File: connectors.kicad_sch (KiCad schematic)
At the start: 13 parts, among them J1 RCJ-017, J2 USB4105-GF-A-120, J3 Conn_01x02_Pin, J4 Conn_01x02_Pin

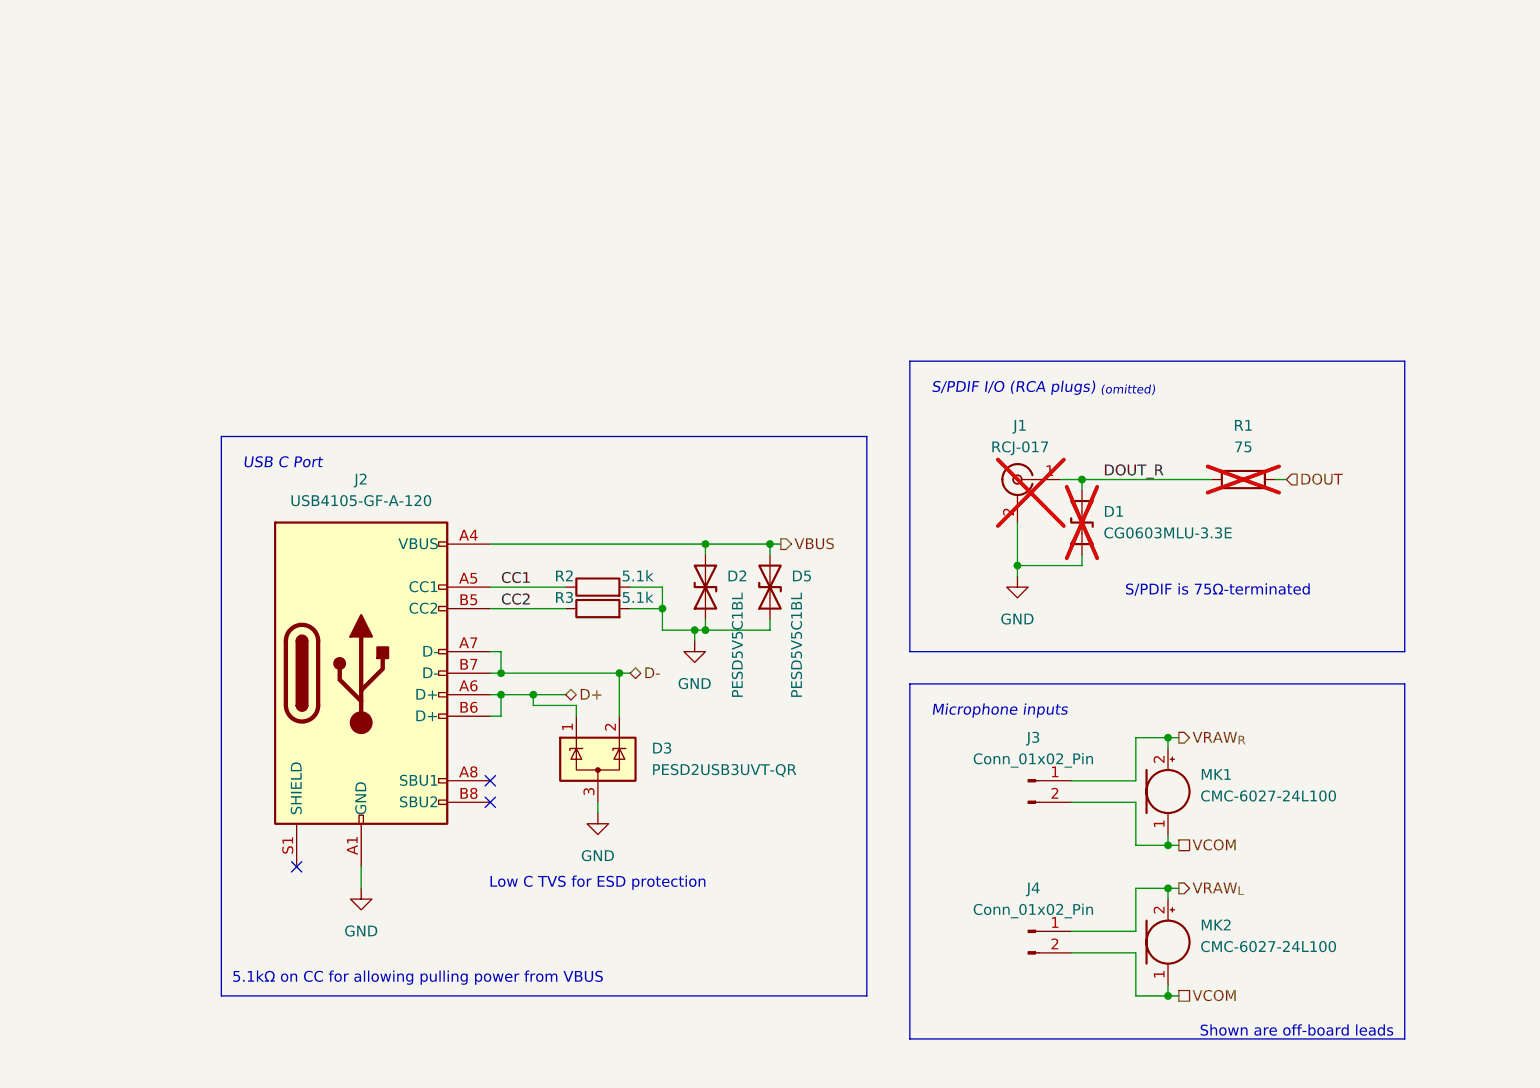
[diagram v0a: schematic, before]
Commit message: Redid schematic and component values according to new recalculations
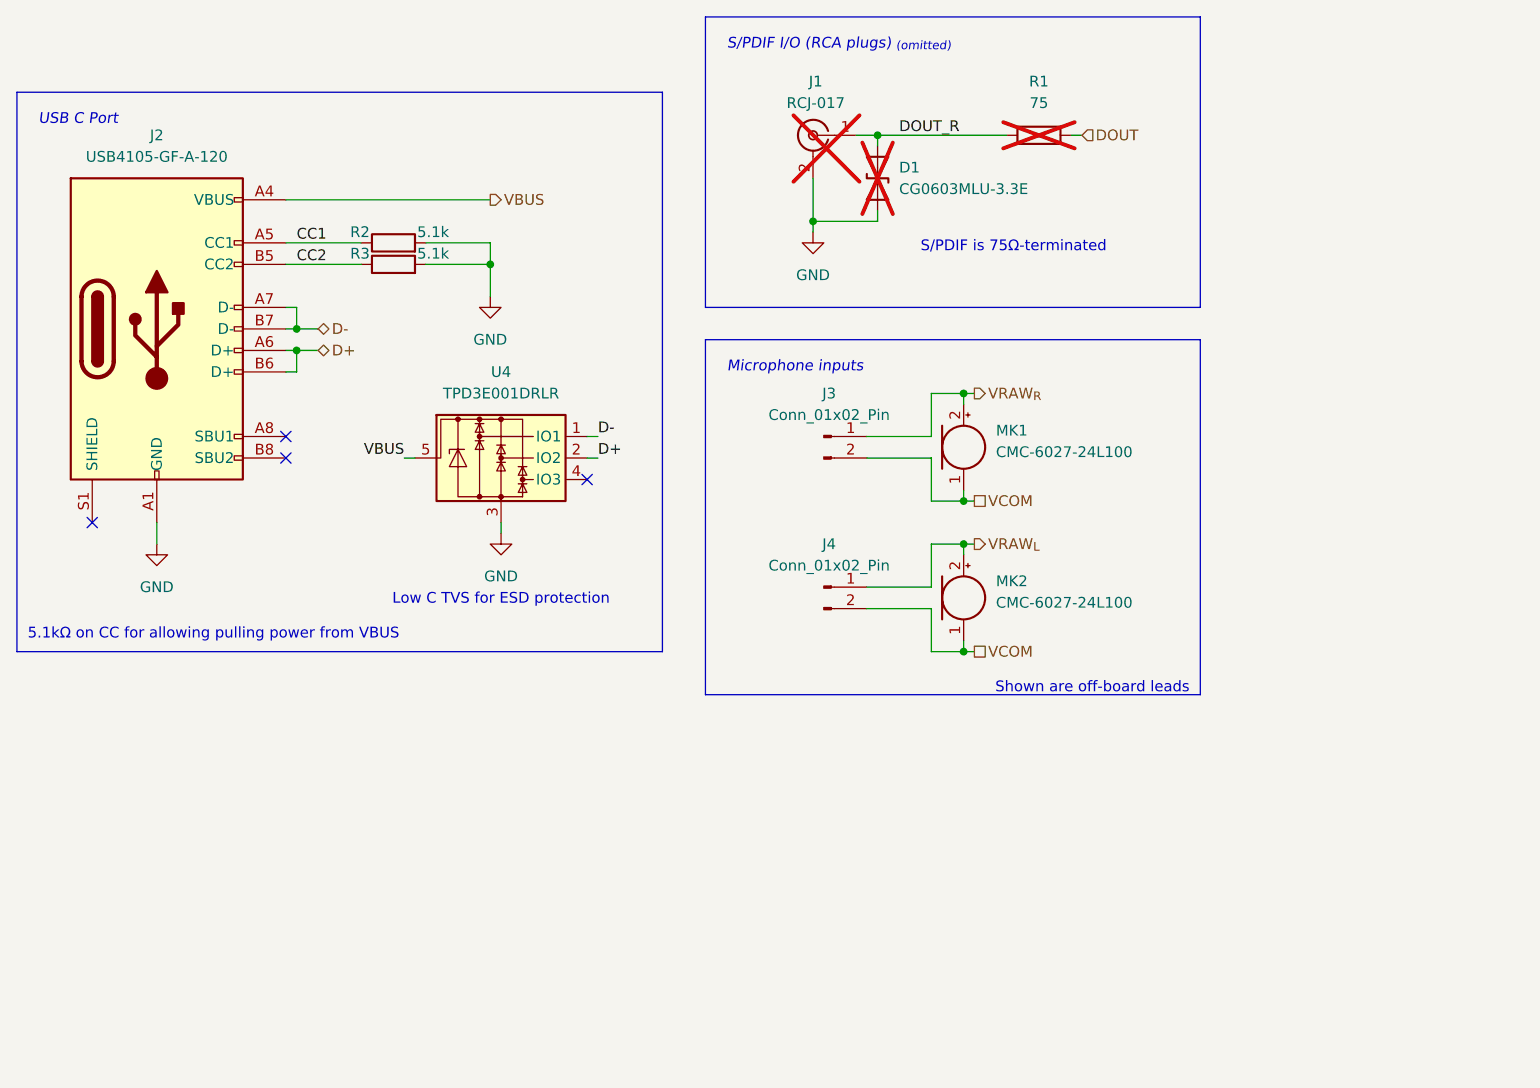
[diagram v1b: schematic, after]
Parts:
- removed D2, D5: PESD5V5C1BL, Diode_SMD:D_SOD-882, symbol Device:D_TVS
- removed D3: PESD2USB3UVT-QR, Package_TO_SOT_SMD:SOT-23-3, symbol Power_Protection:ESDA5V3L
- added U4: TPD3E001DRLR, Package_TO_SOT_SMD:SOT-553, symbol Power_Protection:TPD3E001DRLR
- J2: footprint Connector_USB:USB_C_Receptacle_GCT_USB4105-xx-A_16P_TopMnt_Horizontal -> Connector_USB:USB_C_Receptacle_GCT_USB4085; Mouser Part Number 640-USB4105-GF-A-120 -> 640-USB4085-GF-A
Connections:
- net D+: now also U4.2 (IO2)
- net D-: now also U4.1 (IO1)
- net GND: now also U4.3
- net VBUS: now also U4.5
- no-connect marks 3 -> 4
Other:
- moved on the sheet: D1, J1, J2, J3, J4, MK1, MK2, R1, R2, R3

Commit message: Add buttons for device control + various other changes
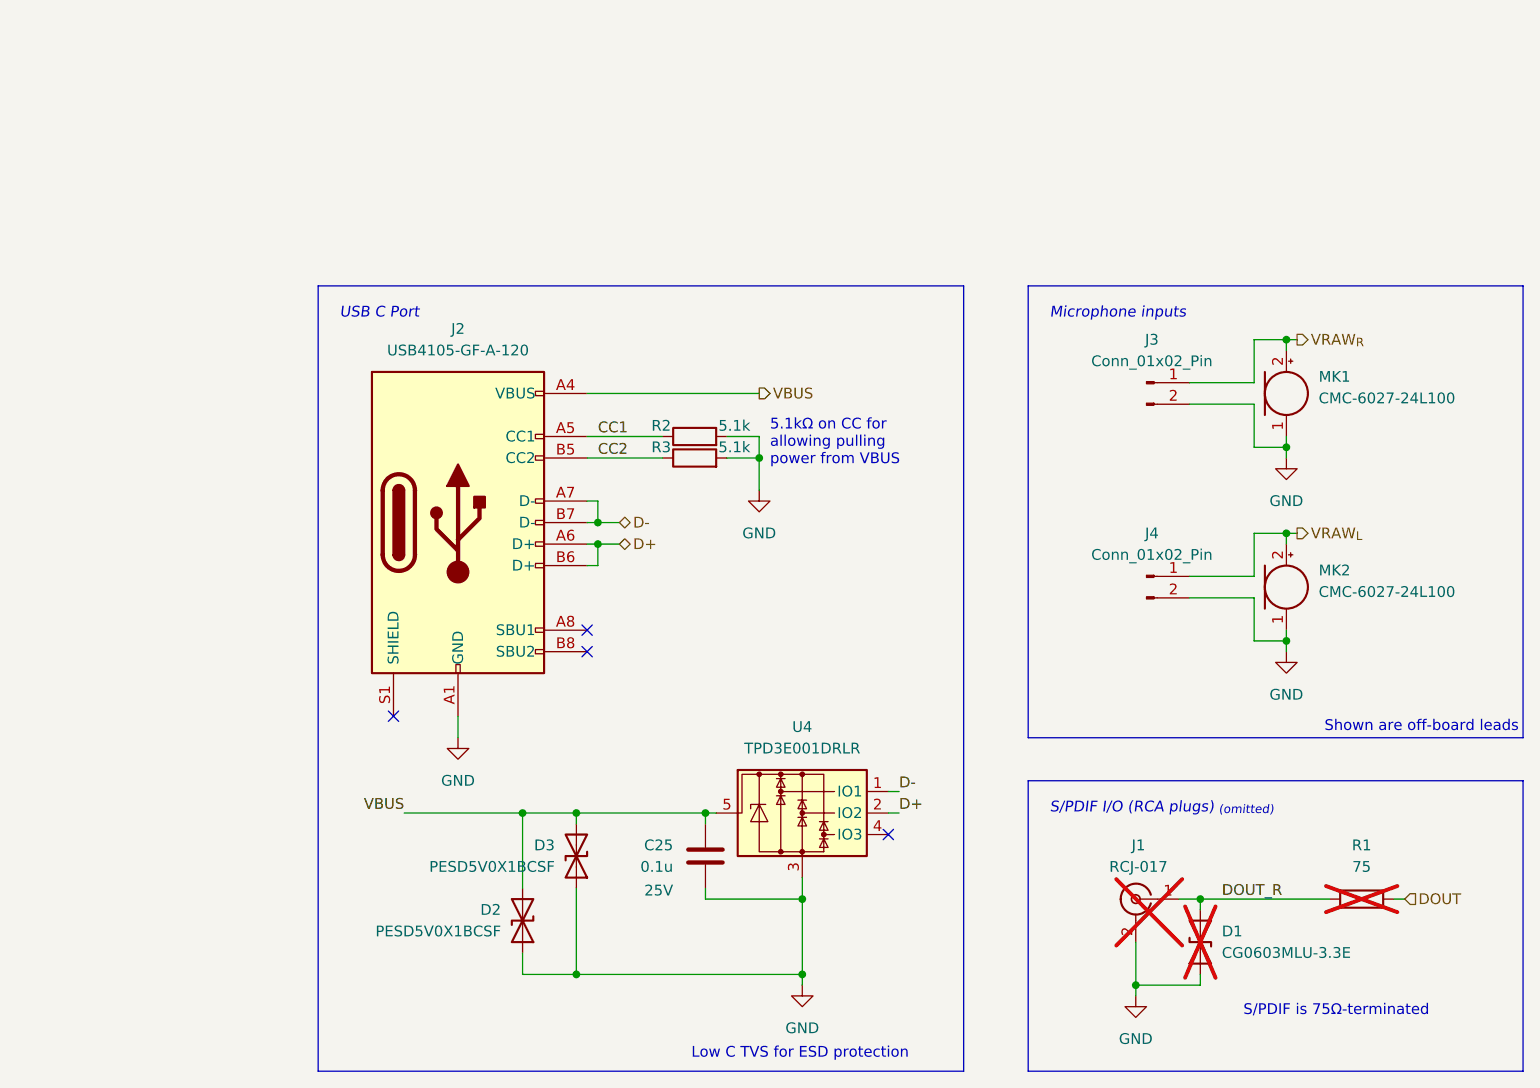
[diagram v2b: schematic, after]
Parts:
- added C25: 0.1u, Capacitor_SMD:C_0603_1608Metric_Pad1.08x0.95mm_HandSolder, symbol Device:C
- added D2, D3: PESD5V0X1BCSF, Diode_SMD:D_0603_1608Metric_Pad1.05x0.95mm_HandSolder, symbol Device:D_TVS
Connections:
- net VCOM is gone; now on net GND: J3.2 (Pin_2), J4.2 (Pin_2), MK1.1 (-), MK2.1 (-)
- net GND: now also C25.1, D2.1 (A1), D3.1 (A1)
- net VBUS: now also C25.2, D2.2 (A2), D3.2 (A2)
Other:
- moved on the sheet: D1, J1, J2, J3, J4, MK1, MK2, R1, R2, R3, U4
